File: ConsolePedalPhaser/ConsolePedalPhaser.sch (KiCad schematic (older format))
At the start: 6 parts, among them J1 Conn_02x25_Counter_Clockwise

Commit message: started to build schematic
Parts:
- added C1, C?: 0.01uF, symbol Device:C
- added C2, C3, C4, C5, C?: 0.047uF, symbol Device:C
- added C? (x2): 10uF, symbol Device:CP
- added D?: 1N4001, Diode_THT:D_DO-41_SOD81_P10.16mm_Horizontal, symbol Diode:1N4001
- added D?: 5.1V, symbol Device:D_Zener
- added Q1, Q2, Q? (x2): 2N5457, symbol Device:Q_NJFET_DSG
- added R1, R3, R?: 470K, Resistor_THT:R_Axial_DIN0207_L6.3mm_D2.5mm_P10.16mm_Horizontal, symbol Device:R
- added R10, R12, R13, R14, R2, R4, R5, R8, R9, R?: 10K, Resistor_THT:R_Axial_DIN0207_L6.3mm_D2.5mm_P10.16mm_Horizontal, symbol Device:R
- added R16, R17, R? (x2): 150K, Resistor_THT:R_Axial_DIN0207_L6.3mm_D2.5mm_P10.16mm_Horizontal, symbol Device:R
- added R28, R6, R? (x3): 22K, Resistor_THT:R_Axial_DIN0207_L6.3mm_D2.5mm_P10.16mm_Horizontal, symbol Device:R
- added R?: 1M, Resistor_THT:R_Axial_DIN0207_L6.3mm_D2.5mm_P10.16mm_Horizontal, symbol Device:R
- added R?: 3.9M, Resistor_THT:R_Axial_DIN0207_L6.3mm_D2.5mm_P10.16mm_Horizontal, symbol Device:R
- added R?: 4.7K, Resistor_THT:R_Axial_DIN0207_L6.3mm_D2.5mm_P10.16mm_Horizontal, symbol Device:R
- added RV?: Trim, symbol Device:R_POT
- added RV?: Speed, symbol Device:R_POT
- added U1, U2, U3: TL072, symbol Amplifier_Operational:TL072
- renumbered D1 to D?, D2 to D?, R3 to R?
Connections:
- net +9V: now also R?.1, U1.8 (V+), U2.8 (V+), U3.8 (V+)
- net GND: now also C?.2, C?.2, D?.2 (A), D?.2 (A), R1.1, RV?.3, U1.4 (V-), U2.4 (V-), U3.4 (V-)
- net Input: now also C1.2, R1.2
- new net: C1.1, R2.1
- new net: R2.2, R3.2, U1.3 (+)
- new net: C2.2, R16.1, R4.1, U1.1, U1.2 (-)
- new net: C3.1, Q2.1 (D), R?.1, U2.5 (+)
- new net: R28.1, R8.2, R9.1, U2.6 (-)
- new net: C4.2, R10.1, R9.2, U2.7
- new net: C2.1, Q1.1 (D), R6.1, U2.3 (+)
- new net: R4.2, R5.1, U2.2 (-)
- new net: C3.2, R5.2, R8.1, U2.1
- new net: R?.1, R?.2, U1.5 (+)
- new net: C?.2, R?.1, U1.6 (-)
- new net: C?.1, R?.1, RV?.3, U1.7
- new net: R?.1, RV?.2
- new net: C?.1, R?.2, R?.2, R?.2
- new net: R?.1, RV?.1, RV?.2
- new net: C4.1, Q?.1 (D), R?.1, U3.3 (+)
- new net: R10.2, R12.1, U3.2 (-)
- new net: C5.2, R12.2, R13.1, U3.1
- new net: C5.1, Q?.1 (D), R?.1, U3.5 (+)
- new net: R13.2, R14.1, U3.6 (-)
- new net: R14.2, R17.1, R28.2, U3.7
- new net: R16.2, R17.2
- new net +5V: C?.1, C?.1, D?.1 (K), D?.1 (K), Q1.2 (S), Q2.2 (S), Q?.2 (S), Q?.2 (S), R3.1, R6.2, R?.2, R?.2, R?.2, R?.2, R?.2, RV?.1
- new net VBIAS: C?.2, Q1.3 (G), Q2.3 (G), Q?.3 (G), Q?.3 (G), R?.1, R?.2
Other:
- moved on the sheet: D?, H1, H2, J1, R?

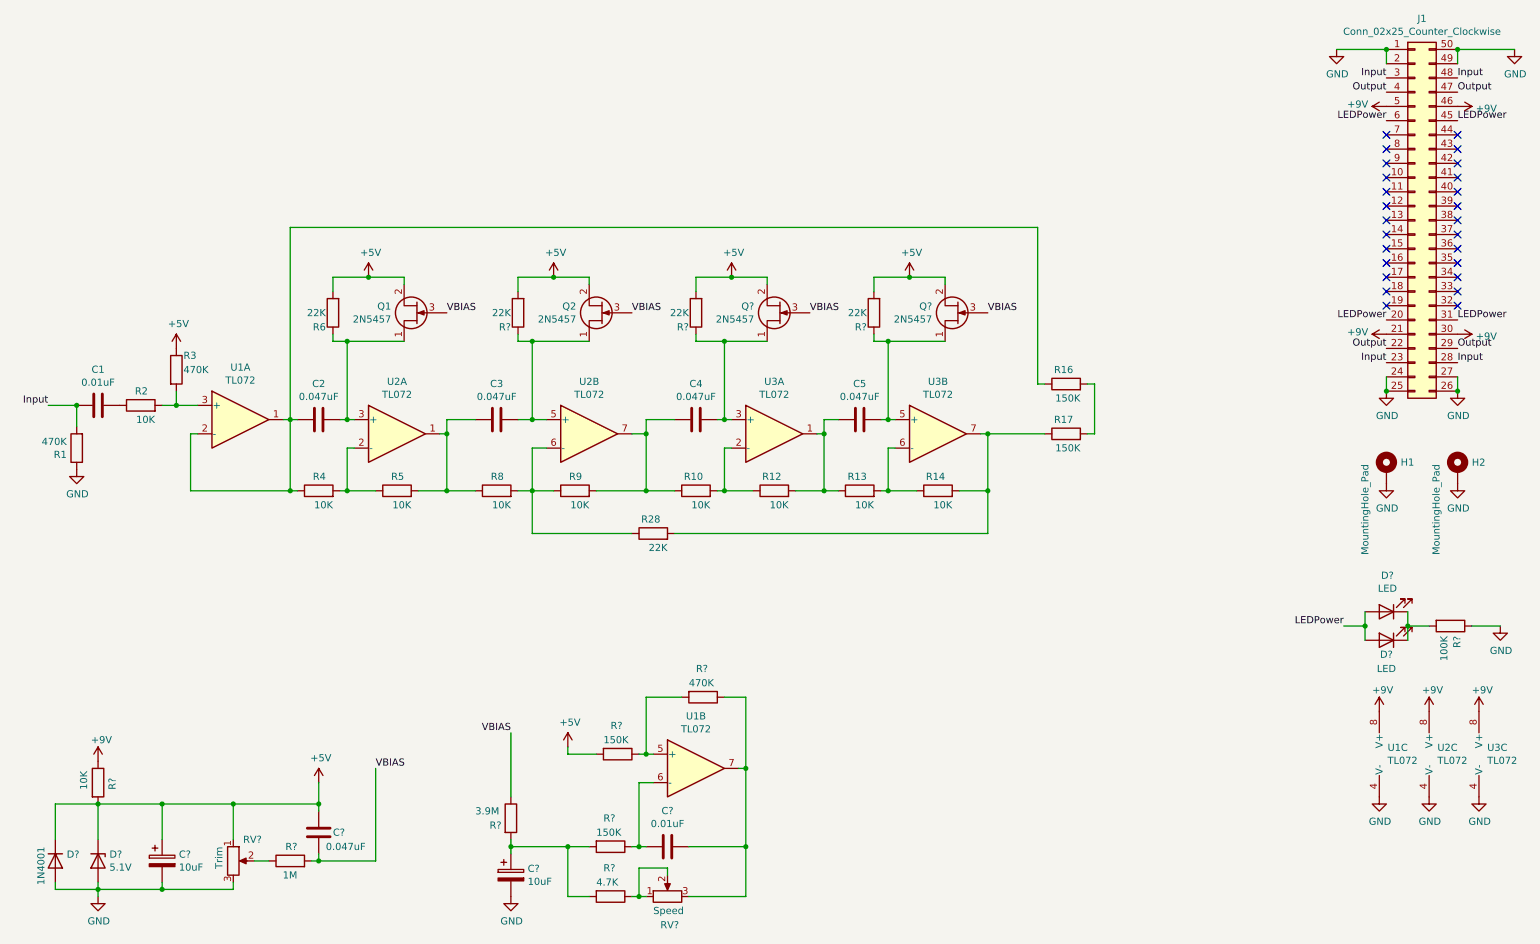
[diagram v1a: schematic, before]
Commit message: Added more to schematic
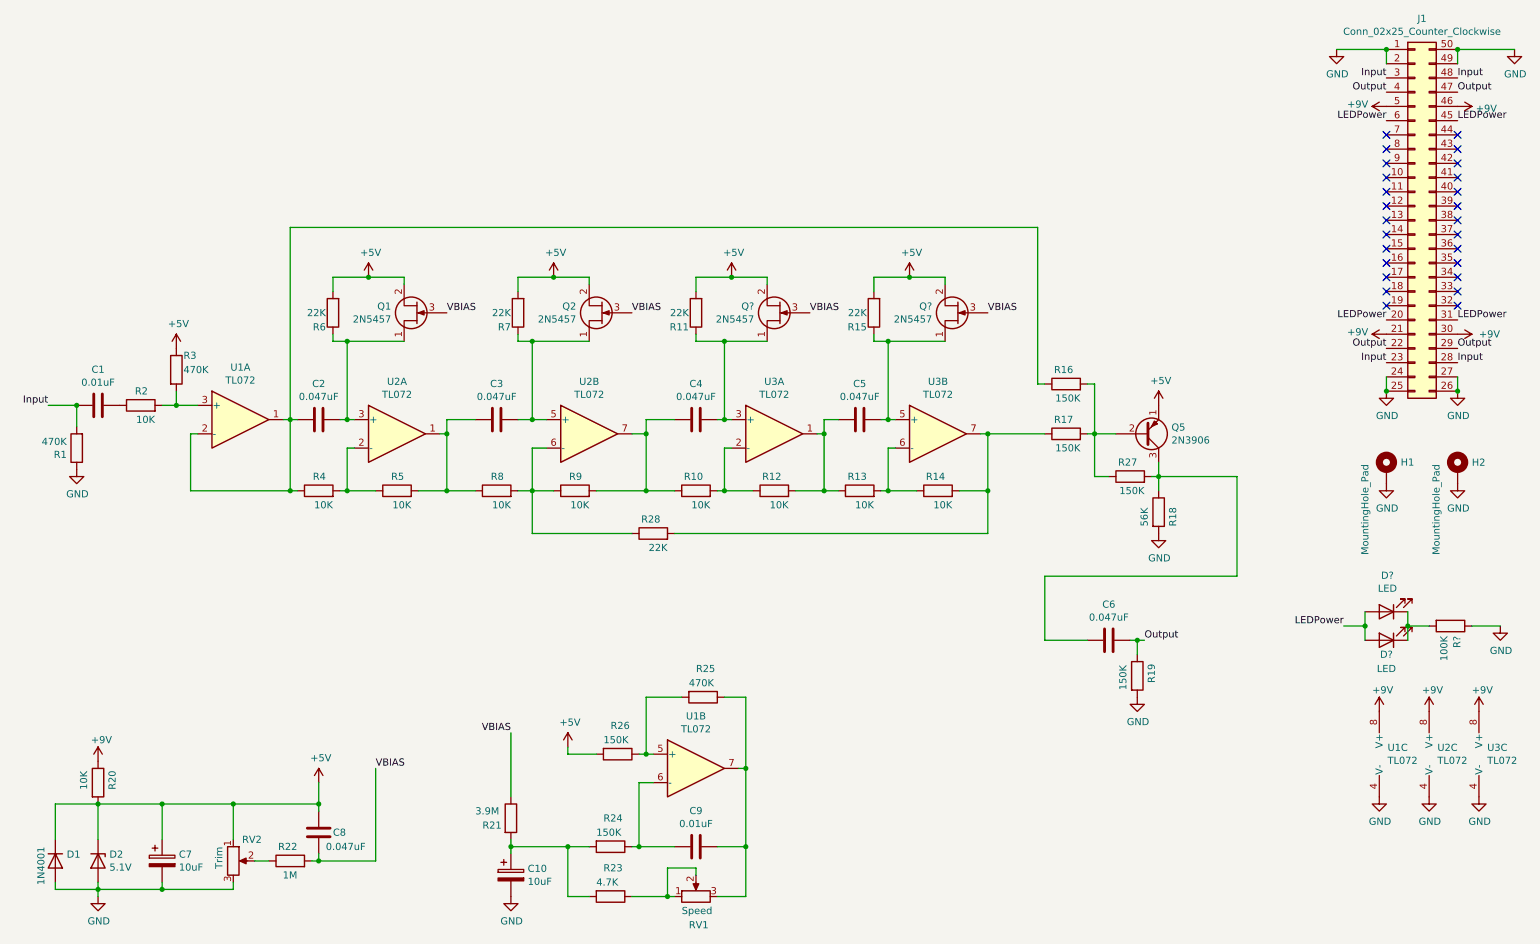
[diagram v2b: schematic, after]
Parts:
- added C6: 0.047uF, symbol Device:C
- added Q5: 2N3906, Package_TO_SOT_THT:TO-92_Inline, symbol Transistor_BJT:2N3906
- added R18: 56K, Resistor_THT:R_Axial_DIN0207_L6.3mm_D2.5mm_P10.16mm_Horizontal, symbol Device:R
- added R19, R27: 150K, Resistor_THT:R_Axial_DIN0207_L6.3mm_D2.5mm_P10.16mm_Horizontal, symbol Device:R
- gave numbers to parts that had none: 18
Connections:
- net +5V: now also Q5.1 (E)
- net GND: now also R18.2, R19.2
- net Output: now also C6.1, R19.1
- net at R16.2, R17.2: now also Q5.2 (B), R27.1
- new net: C6.2, Q5.3 (C), R18.1, R27.2
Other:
- moved on the sheet: C9, RV1
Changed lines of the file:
@@
 P 10600 2800
 F 0 "#PWR011" H 10600 2650 50  0001 C CNN
-F 1 "+9V" V 10615 2928 50  0000 L CNN
+F 1 "+9V" V 10600 2950 50  0000 L CNN
 F 2 "" H 10600 2800 50  0001 C CNN
 F 3 "" H 10600 2800 50  0001 C CNN
@@
 $EndComp
 $Comp
-L Diode:1N4001 D?
+L Diode:1N4001 D1
 U 1 1 60E945D8
 P 750 6500
-F 0 "D?" V 704 6580 50  0000 L CNN
+F 0 "D1" V 704 6580 50  0000 L CNN
 F 1 "1N4001" H 650 6400 50  0000 L CNN
 F 2 "Diode_THT:D_DO-41_SOD81_P10.16mm_Horizontal" H 750 6325 50  0001 C CNN
@@
 $EndComp
 $Comp
-L Device:D_Zener D?
+L Device:D_Zener D2
 U 1 1 60E964C4
 P 1050 6500
-F 0 "D?" V 1004 6580 50  0000 L CNN
+F 0 "D2" V 1004 6580 50  0000 L CNN
 F 1 "5.1V" V 1095 6580 50  0000 L CNN
 F 2 "" H 1050 6500 50  0001 C CNN
@@
 $EndComp
 $Comp
-L Device:CP C?
+L Device:CP C7
 U 1 1 60E98CD9
 P 1500 6500
-F 0 "C?" H 1618 6546 50  0000 L CNN
+F 0 "C7" H 1618 6546 50  0000 L CNN
 F 1 "10uF" H 1618 6455 50  0000 L CNN
 F 2 "" H 1538 6350 50  0001 C CNN
@@
 	1500 6700 1050 6700
 $Comp
-L Device:R_POT RV?
+L Device:R_POT RV2
 U 1 1 60EA0631
 P 2000 6500
-F 0 "RV?" H 2200 6650 50  0000 R CNN
+F 0 "RV2" H 2200 6650 50  0000 R CNN
 F 1 "Trim" V 1900 6600 50  0000 R CNN
 F 2 "" H 2000 6500 50  0001 C CNN
@@
 Connection ~ 1500 6700
 $Comp
-L Device:R R?
+L Device:R R22
 U 1 1 60EA6DD9
 P 2400 6500
-F 0 "R?" V 2500 6450 50  0000 L CNN
+F 0 "R22" V 2500 6450 50  0000 L CNN
 F 1 "1M" V 2300 6450 50  0000 L CNN
 F 2 "Resistor_THT:R_Axial_DIN0207_L6.3mm_D2.5mm_P10.16mm_Horizontal" V 2330 6500 50  0001 C CNN
@@
 	2250 6500 2150 6500
 $Comp
-L Device:C C?
+L Device:C C8
 U 1 1 60EA9CFB
 P 2600 6300
-F 0 "C?" H 2700 6300 50  0000 L CNN
+F 0 "C8" H 2700 6300 50  0000 L CNN
 F 1 "0.047uF" H 2650 6200 50  0000 L CNN
 F 2 "" H 2638 6150 50  0001 C CNN
@@
 Connection ~ 1050 6100
 $Comp
-L Device:R R?
+L Device:R R20
 U 1 1 60EB1A58
 P 1050 5950
-F 0 "R?" V 1150 5900 50  0000 L CNN
+F 0 "R20" V 1150 5900 50  0000 L CNN
 F 1 "10K" V 950 5900 50  0000 L CNN
 F 2 "Resistor_THT:R_Axial_DIN0207_L6.3mm_D2.5mm_P10.16mm_Horizontal" V 980 5950 50  0001 C CNN
@@
 Connection ~ 2600 6500
 $Comp
-L Device:CP C?
+L Device:CP C10
 U 1 1 60EC5EC4
 P 3950 6600
-F 0 "C?" H 4068 6646 50  0000 L CNN
+F 0 "C10" H 4068 6646 50  0000 L CNN
 F 1 "10uF" H 4068 6555 50  0000 L CNN
 F 2 "" H 3988 6450 50  0001 C CNN
@@
 $EndComp
 $Comp
-L Device:R R?
+L Device:R R21
 U 1 1 60EC6F2A
 P 3950 6200
-F 0 "R?" H 3800 6150 50  0000 L CNN
+F 0 "R21" H 3750 6150 50  0000 L CNN
 F 1 "3.9M" H 3700 6250 50  0000 L CNN
 F 2 "Resistor_THT:R_Axial_DIN0207_L6.3mm_D2.5mm_P10.16mm_Horizontal" V 3880 6200 50  0001 C CNN
@@
 $EndComp
 $Comp
-L Device:R R?
+L Device:R R24
 U 1 1 60ECAD97
 P 4650 6400
-F 0 "R?" V 4450 6350 50  0000 L CNN
+F 0 "R24" V 4450 6350 50  0000 L CNN
 F 1 "150K" V 4550 6300 50  0000 L CNN
 F 2 "Resistor_THT:R_Axial_DIN0207_L6.3mm_D2.5mm_P10.16mm_Horizontal" V 4580 6400 50  0001 C CNN
@@
 	3950 6400 3950 6450
 $Comp
-L Device:R R?
+L Device:R R23
 U 1 1 60ECEFB3
 P 4650 6750
-F 0 "R?" V 4450 6700 50  0000 L CNN
+F 0 "R23" V 4450 6700 50  0000 L CNN
 F 1 "4.7K" V 4550 6650 50  0000 L CNN
 F 2 "Resistor_THT:R_Axial_DIN0207_L6.3mm_D2.5mm_P10.16mm_Horizontal" V 4580 6750 50  0001 C CNN
@@
 	4350 6400 3950 6400
 $Comp
-L Device:R_POT RV?
+L Device:R_POT RV1
 U 1 1 60ED150F
-P 5050 6750
-F 0 "RV?" V 4850 6800 50  0000 R CNN
-F 1 "Speed" V 4950 6850 50  0000 R CNN
-F 2 "" H 5050 6750 50  0001 C CNN
-F 3 "~" H 5050 6750 50  0001 C CNN
-	1    5050 6750
-	0    -1   -1   0
-$EndComp
-Wire Wire Line
-	4900 6750 4850 6750
-Wire Wire Line
-	4850 6750 4850 6550
-Wire Wire Line
-	4850 6550 5050 6550
-Wire Wire Line
-	5050 6550 5050 6600
-Connection ~ 4850 6750
-Wire Wire Line
-	4850 6750 4800 6750
-$Comp
-L Device:C C?
+P 5250 6750
+F 0 "RV1" V 5050 6800 50  0000 R CNN
+F 1 "Speed" V 5150 6850 50  0000 R CNN
+F 2 "" H 5250 6750 50  0001 C CNN
+F 3 "~" H 5250 6750 50  0001 C CNN
+	1    5250 6750
+	0    -1   -1   0
+$EndComp
+$Comp
+L Device:C C9
 U 1 1 60ED696D
-P 5050 6400
-F 0 "C?" V 4798 6400 50  0000 C CNN
-F 1 "0.01uF" V 4889 6400 50  0000 C CNN
-F 2 "" H 5088 6250 50  0001 C CNN
-F 3 "~" H 5050 6400 50  0001 C CNN
-	1    5050 6400
-	0    1    1    0
-$EndComp
-Wire Wire Line
-	4900 6400 4850 6400
+P 5250 6400
+F 0 "C9" V 4998 6400 50  0000 C CNN
+F 1 "0.01uF" V 5089 6400 50  0000 C CNN
+F 2 "" H 5288 6250 50  0001 C CNN
+F 3 "~" H 5250 6400 50  0001 C CNN
+	1    5250 6400
+	0    1    1    0
+$EndComp
 Wire Wire Line
 	4950 5950 4850 5950
 Wire Wire Line
 	4850 5950 4850 6400
-Connection ~ 4850 6400
 Wire Wire Line
 	4850 6400 4800 6400
 $Comp
-L Device:R R?
+L Device:R R26
 U 1 1 60EE699E
 P 4700 5750
-F 0 "R?" V 4500 5700 50  0000 L CNN
+F 0 "R26" V 4500 5700 50  0000 L CNN
 F 1 "150K" V 4600 5650 50  0000 L CNN
 F 2 "Resistor_THT:R_Axial_DIN0207_L6.3mm_D2.5mm_P10.16mm_Horizontal" V 4630 5750 50  0001 C CNN
@@
 Wire Wire Line
 	5550 5850 5600 5850
-Wire Wire Line
-	5600 5850 5600 6400
-Wire Wire Line
-	5600 6750 5200 6750
-Wire Wire Line
-	5200 6400 5600 6400
-Connection ~ 5600 6400
-Wire Wire Line
-	5600 6400 5600 6750
-$Comp
-L Device:R R?
+$Comp
+L Device:R R25
 U 1 1 60EF5B4C
 P 5300 5350
-F 0 "R?" V 5100 5300 50  0000 L CNN
+F 0 "R25" V 5100 5300 50  0000 L CNN
 F 1 "470K" V 5200 5250 50  0000 L CNN
 F 2 "Resistor_THT:R_Axial_DIN0207_L6.3mm_D2.5mm_P10.16mm_Horizontal" V 5230 5350 50  0001 C CNN
@@
 $EndComp
 $Comp
-L Device:R R?
+L Device:R R7
 U 1 1 60F4ADE7
 P 4000 2650
-F 0 "R?" H 4050 2750 50  0000 L CNN
+F 0 "R7" H 4050 2750 50  0000 L CNN
 F 1 "22K" H 4050 2650 50  0000 L CNN
 F 2 "Resistor_THT:R_Axial_DIN0207_L6.3mm_D2.5mm_P10.16mm_Horizontal" V 3930 2650 50  0001 C CNN
@@
 $EndComp
 $Comp
-L Device:R R?
+L Device:R R11
 U 1 1 6101F734
 P 5250 2650
-F 0 "R?" H 5300 2750 50  0000 L CNN
+F 0 "R11" H 5300 2750 50  0000 L CNN
 F 1 "22K" H 5300 2650 50  0000 L CNN
 F 2 "Resistor_THT:R_Axial_DIN0207_L6.3mm_D2.5mm_P10.16mm_Horizontal" V 5180 2650 50  0001 C CNN
@@
 $EndComp
 $Comp
-L Device:R R?
+L Device:R R15
 U 1 1 6105AE5C
 P 6500 2650
-F 0 "R?" H 6550 2750 50  0000 L CNN
+F 0 "R15" H 6550 2750 50  0000 L CNN
 F 1 "22K" H 6550 2650 50  0000 L CNN
 F 2 "Resistor_THT:R_Axial_DIN0207_L6.3mm_D2.5mm_P10.16mm_Horizontal" V 6430 2650 50  0001 C CNN
@@
 	7300 4200 7300 3900
 Connection ~ 7300 3900
+$Comp
+L Transistor_BJT:2N3906 Q5
+U 1 1 60E78932
+P 8400 3500
+F 0 "Q5" H 8590 3454 50  0000 L CNN
+F 1 "2N3906" H 8590 3545 50  0000 L CNN
+F 2 "Package_TO_SOT_THT:TO-92_Inline" H 8600 3425 50  0001 L CIN
+F 3 "https://www.onsemi.com/pub/Collateral/2N3906-D.PDF" H 8400 3500 50  0001 L CNN
+	1    8400 3500
+	1    0    0    1
+$EndComp
+$Comp
+L Device:R R27
+U 1 1 60E810C5
+P 8300 3800
+F 0 "R27" V 8400 3750 50  0000 L CNN
+F 1 "150K" V 8200 3700 50  0000 L CNN
+F 2 "Resistor_THT:R_Axial_DIN0207_L6.3mm_D2.5mm_P10.16mm_Horizontal" V 8230 3800 50  0001 C CNN
+F 3 "~" H 8300 3800 50  0001 C CNN
+	1    8300 3800
+	0    -1   -1   0
+$EndComp
+Wire Wire Line
+	8150 3800 8050 3800
+Wire Wire Line
+	8050 3800 8050 3500
+Connection ~ 8050 3500
+Wire Wire Line
+	8200 3500 8050 3500
+Wire Wire Line
+	8450 3800 8500 3800
+Wire Wire Line
+	8500 3800 8500 3700
+$Comp
+L power:+5V #PWR?
+U 1 1 60EA2C6F
+P 8500 3300
+F 0 "#PWR?" H 8500 3150 50  0001 C CNN
+F 1 "+5V" H 8515 3473 50  0000 C CNN
+F 2 "" H 8500 3300 50  0001 C CNN
+F 3 "" H 8500 3300 50  0001 C CNN
+	1    8500 3300
+	1    0    0    -1
+$EndComp
+$Comp
+L Device:R R18
+U 1 1 60EA4FC7
+P 8500 4050
+F 0 "R18" V 8600 3950 50  0000 L CNN
+F 1 "56K" V 8400 3950 50  0000 L CNN
+F 2 "Resistor_THT:R_Axial_DIN0207_L6.3mm_D2.5mm_P10.16mm_Horizontal" V 8430 4050 50  0001 C CNN
+F 3 "~" H 8500 4050 50  0001 C CNN
+	1    8500 4050
+	1    0    0    -1
+$EndComp
+Wire Wire Line
+	8500 3900 8500 3800
+Connection ~ 8500 3800
+$Comp
+L power:GND #PWR?
+U 1 1 60EB03D5
+P 8500 4200
+F 0 "#PWR?" H 8500 3950 50  0001 C CNN
+F 1 "GND" H 8505 4027 50  0000 C CNN
+F 2 "" H 8500 4200 50  0001 C CNN
+F 3 "" H 8500 4200 50  0001 C CNN
+	1    8500 4200
+	1    0    0    -1
+$EndComp
+$Comp
+L Device:C C6
+U 1 1 60EB1DE3
+P 8150 4950
+F 0 "C6" V 7898 4950 50  0000 C CNN
+F 1 "0.047uF" V 7989 4950 50  0000 C CNN
+F 2 "" H 8188 4800 50  0001 C CNN
+F 3 "~" H 8150 4950 50  0001 C CNN
+	1    8150 4950
+	0    1    1    0
+$EndComp
+Text Label 8400 4950 0    50   ~ 0
+Output
+Wire Wire Line
+	8400 4950 8350 4950
+$Comp
+L Device:R R19
+U 1 1 60EBC537
+P 8350 5200
+F 0 "R19" V 8450 5150 50  0000 L CNN
+F 1 "150K" V 8250 5100 50  0000 L CNN
+F 2 "Resistor_THT:R_Axial_DIN0207_L6.3mm_D2.5mm_P10.16mm_Horizontal" V 8280 5200 50  0001 C CNN
+F 3 "~" H 8350 5200 50  0001 C CNN
+	1    8350 5200
+	1    0    0    -1
+$EndComp
+Wire Wire Line
+	8350 5050 8350 4950
+Connection ~ 8350 4950
+Wire Wire Line
+	8350 4950 8300 4950
+$Comp
+L power:GND #PWR?
+U 1 1 60EC61D4
+P 8350 5350
+F 0 "#PWR?" H 8350 5100 50  0001 C CNN
+F 1 "GND" H 8355 5177 50  0000 C CNN
+F 2 "" H 8350 5350 50  0001 C CNN
+F 3 "" H 8350 5350 50  0001 C CNN
+	1    8350 5350
+	1    0    0    -1
+$EndComp
+Wire Wire Line
+	8000 4950 7700 4950
+Wire Wire Line
+	7700 4950 7700 4500
+Wire Wire Line
+	7700 4500 9050 4500
+Wire Wire Line
+	9050 4500 9050 3800
+Wire Wire Line
+	9050 3800 8500 3800
+Wire Wire Line
+	5600 5850 5600 6400
+Wire Wire Line
+	5100 6400 4850 6400
+Connection ~ 4850 6400
+Wire Wire Line
+	5400 6400 5600 6400
+Connection ~ 5600 6400
+Wire Wire Line
+	5600 6400 5600 6750
+Wire Wire Line
+	5250 6600 5250 6550
+Wire Wire Line
+	5250 6550 5050 6550
+Wire Wire Line
+	5050 6550 5050 6750
+Wire Wire Line
+	5050 6750 5100 6750
+Wire Wire Line
+	4800 6750 5050 6750
+Connection ~ 5050 6750
+Wire Wire Line
+	5400 6750 5600 6750
 $EndSCHEMATC

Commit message: Assigned all footprints and generated netlist
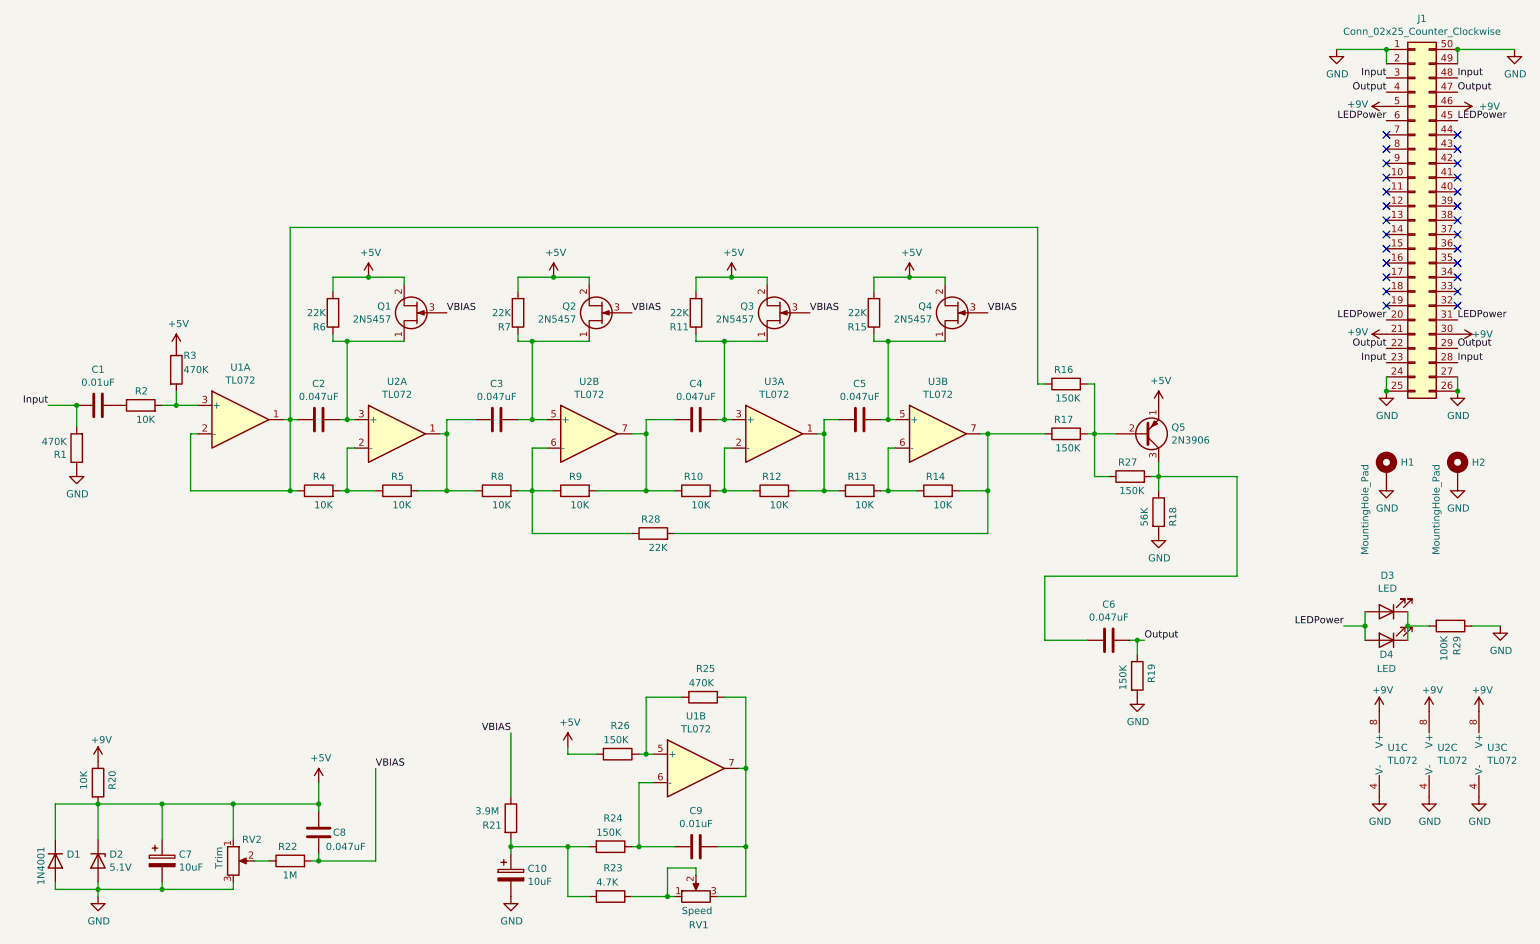
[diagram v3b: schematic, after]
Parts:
- C1, C2, C3, C4, C5, C6, C8, C9: footprint (none) -> libraries:C_Flat_L7.2_H6.5
- C10, C7: footprint (none) -> libraries:CP_Radial_D6.3mm_P2.50mm_L11.0mm
- D2: footprint (none) -> Diode_THT:D_DO-35_SOD27_P7.62mm_Horizontal
- Q1, Q2: footprint (none) -> Package_TO_SOT_THT:TO-92_Inline
- Q3, Q4: renamed from Q?; footprint (none) -> Package_TO_SOT_THT:TO-92_Inline
- RV1, RV2: footprint (none) -> Potentiometer_THT:Potentiometer_Bourns_PTV09A-1_Single_Vertical
- U1, U2, U3: footprint (none) -> Package_DIP:DIP-8_W7.62mm_Socket
- gave numbers to parts that had none: 3

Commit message: Started to move around components
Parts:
- RV2: footprint Potentiometer_THT:Potentiometer_Bourns_PTV09A-1_Single_Vertical -> Potentiometer_THT:Potentiometer_Bourns_3386F_Vertical
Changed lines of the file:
@@
 F 0 "RV2" H 2200 6650 50  0000 R CNN
 F 1 "Trim" V 1900 6600 50  0000 R CNN
-F 2 "Potentiometer_THT:Potentiometer_Bourns_PTV09A-1_Single_Vertical" H 2000 6500 50  0001 C CNN
+F 2 "Potentiometer_THT:Potentiometer_Bourns_3386F_Vertical" H 2000 6500 50  0001 C CNN
 F 3 "~" H 2000 6500 50  0001 C CNN
 	1    2000 6500
